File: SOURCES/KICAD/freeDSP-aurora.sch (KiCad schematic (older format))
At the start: 76 parts, among them IC101 IC_ADAU1452, IC102 IC_25AA1024, IC103 IC_TLE2426ID, IC104 IC_ADM811TARTZ, IC105 IC_LM1117MP-5.0, IC106 IC_NCP1117LPST33, IC107 IC_LM1117MP-5.0, Q101 Q_STD2805, X101 MicroMatch14, X102 HDR_02x08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

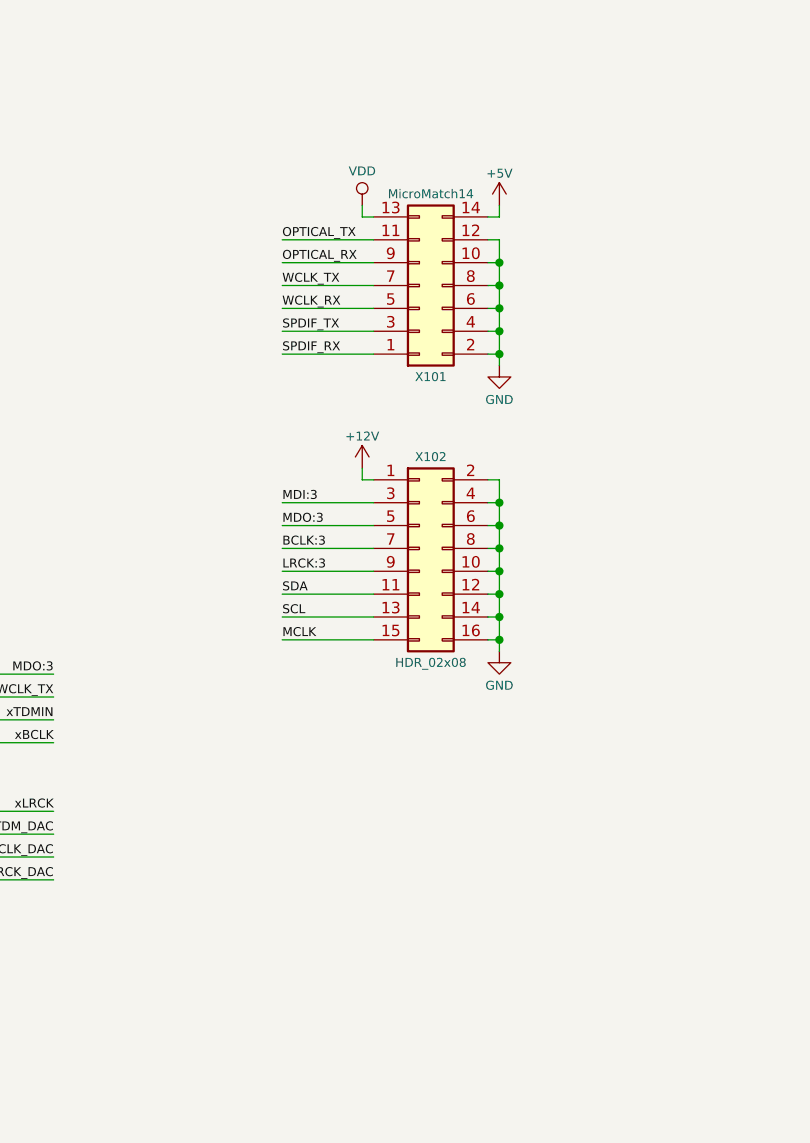
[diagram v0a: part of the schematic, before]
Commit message: Optimized ground plane
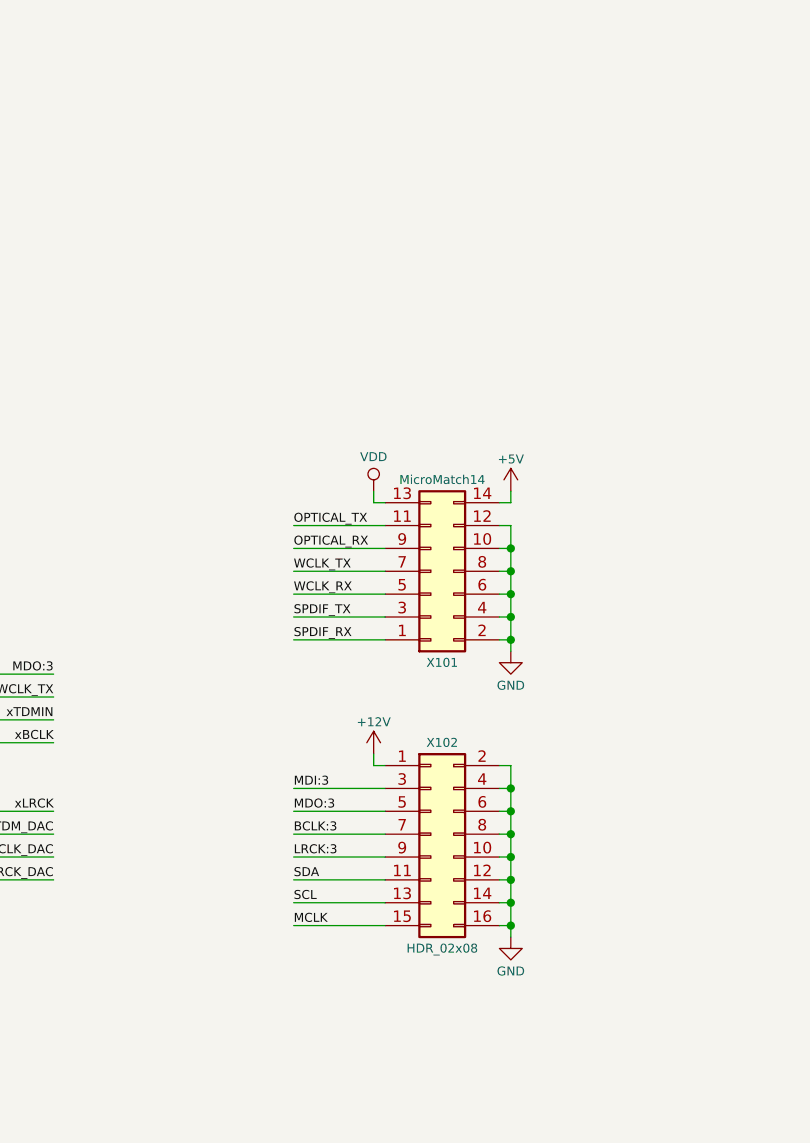
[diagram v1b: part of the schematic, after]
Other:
- moved on the sheet: X101, X102

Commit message: Updated BOM
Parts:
- B101, B102, B103, B104: Manufacturer (none) -> -; pn (none) -> -
- C101: manf_num GRM21BR61E106MA73L -> (none)
- R101, R102, R104, R105: digikey ??? -> TC164J-33CT-ND
- R108: value 100R -> RES_100R_1%_0.125W_Thick_0805; digikey ??? -> 311-100CRCT-ND
- R116: value 560R -> RES_560R_1%_0.125W_Thick_0805; Manufacturer (none) -> Yageo; digikey ??? -> 311-560CRCT-ND; pn (none) -> RC0805FR-07560RL
- X101: digikey ??? -> A110871CT-ND
- X102: digikey ??? -> S2011EC-08-ND
- X103: digikey ??? -> WM1732-ND
- X106: Manufacturer (none) -> Wurth Electronics Inc.; Value1 (none) -> HDR-01x02; Value2 (none) -> -; digikey (none) -> 732-5315-ND; pn (none) -> 61300211121
- Y101: digikey ??? -> SER3690CT-ND
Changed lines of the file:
@@
 F 5 "-" H 0   0   50  0001 C CNN "Value2"
 F 6 "-" H 0   0   50  0001 C CNN "digikey"
+F 7 "-" H 0   0   50  0001 C CNN "Manufacturer"
+F 8 "-" H 0   0   50  0001 C CNN "pn"
 	1    15400 9900
 	1    0    0    -1
@@
 F 5 "-" H 0   0   50  0001 C CNN "Value2"
 F 6 "-" H 0   0   50  0001 C CNN "digikey"
+F 7 "-" H 0   0   50  0001 C CNN "Manufacturer"
+F 8 "-" H 0   0   50  0001 C CNN "pn"
 	1    15550 9900
 	1    0    0    -1
@@
 F 5 "-" H 0   0   50  0001 C CNN "Value2"
 F 6 "-" H 0   0   50  0001 C CNN "digikey"
+F 7 "-" H 0   0   50  0001 C CNN "Manufacturer"
+F 8 "-" H 0   0   50  0001 C CNN "pn"
 	1    15700 9900
 	1    0    0    -1
@@
 F 5 "-" H 0   0   50  0001 C CNN "Value2"
 F 6 "-" H 0   0   50  0001 C CNN "digikey"
+F 7 "-" H 0   0   50  0001 C CNN "Manufacturer"
+F 8 "-" H 0   0   50  0001 C CNN "pn"
 	1    15850 9900
 	1    0    0    -1
@@
 P 7200 6450
 F 0 "R108" V 7200 6450 39  0000 C CNN
-F 1 "100R" V 7275 6450 39  0000 C CNN
+F 1 "RES_100R_1%_0.125W_Thick_0805" V 7275 6450 39  0000 C CNN
 F 2 "rklib:C0805-RES" V 7130 6450 50  0001 C CNN
 F 3 "" H 7200 6450 50  0000 C CNN
 F 4 "100R" H 0   0   50  0001 C CNN "Value1"
 F 5 "1% 0.125W Thick" H 0   0   50  0001 C CNN "Value2"
-F 6 "???" H 0   0   50  0001 C CNN "digikey"
+F 6 "311-100CRCT-ND" H 0   0   50  0001 C CNN "digikey"
 F 7 "Yageo" H 0   0   50  0001 C CNN "Manufacturer"
 F 8 "RC0805FR-07100RL" H 0   0   50  0001 C CNN "pn"
@@
 F 4 "24M576" H 0   0   50  0001 C CNN "Value1"
 F 5 "-" H 0   0   50  0001 C CNN "Value2"
-F 6 "???" H 0   0   50  0001 C CNN "digikey"
+F 6 "SER3690CT-ND" H 0   0   50  0001 C CNN "digikey"
 F 7 "EPSON" H 0   0   50  0001 C CNN "Manufacturer"
 F 8 "FA-238 24.5760MB-K3" H 0   0   50  0001 C CNN "pn"
@@
 F 4 "MicroMatch-14" H 50  1250 50  0001 C CNN "Value1"
 F 5 "-" H 50  1250 50  0001 C CNN "Value2"
-F 6 "???" H 50  1250 50  0001 C CNN "digikey"
+F 6 "A110871CT-ND" H 50  1250 50  0001 C CNN "digikey"
 F 7 "TE Connectivity AMP Connectors" H 50  1250 50  0001 C CNN "Manufacturer"
 F 8 "1-215079-4" H 50  1250 50  0001 C CNN "pn"
@@
 F 4 "HDR_02x08" H 50  1250 50  0001 C CNN "Value1"
 F 5 "-" H 50  1250 50  0001 C CNN "Value2"
-F 6 "???" H 50  1250 50  0001 C CNN "digikey"
+F 6 "S2011EC-08-ND" H 50  1250 50  0001 C CNN "digikey"
 F 7 "Sullins Connector Solutions" H 50  1250 50  0001 C CNN "Manufacturer"
 F 8 "PRPC008DAAN-RC" H 50  1250 50  0001 C CNN "pn"
@@
 F 7 "Murata Electronics North America" H 5650 4800 39  0001 C CNN "Manufacturer"
 F 8 "GRM21BR61E106MA73L" H 5650 4800 39  0001 C CNN "pn"
-F 9 "GRM21BR61E106MA73L" H 5650 4800 50  0001 C CNN "manf_num"
 	1    5650 4800
 	0    1    1    0
@@
 F 4 "33R0" V 7650 3000 39  0000 L CNN "Value1"
 F 5 "5% 62,5mW" H 7400 2700 39  0001 C CNN "Value2"
-F 6 "???" H 7400 2600 39  0001 C CNN "digikey"
+F 6 "TC164J-33CT-ND" H 7400 2600 39  0001 C CNN "digikey"
 F 7 "Yageo" H 0   0   50  0001 C CNN "Manufacturer"
 F 8 "TC164-JR-0733RL" H 0   0   50  0001 C CNN "pn"
@@
 F 4 "33R0" V 8550 3000 39  0000 L CNN "Value1"
 F 5 "5% 62,5mW" H 8300 2700 39  0001 C CNN "Value2"
-F 6 "???" H 8300 2600 39  0001 C CNN "digikey"
+F 6 "TC164J-33CT-ND" H 8300 2600 39  0001 C CNN "digikey"
 F 7 "Yageo" H 0   0   50  0001 C CNN "Manufacturer"
 F 8 "TC164-JR-0733RL" H 0   0   50  0001 C CNN "pn"
@@
 F 4 "33R0" V 9650 4700 39  0000 L CNN "Value1"
 F 5 "5% 62,5mW" H 9400 4400 39  0001 C CNN "Value2"
-F 6 "???" H 9400 4300 39  0001 C CNN "digikey"
+F 6 "TC164J-33CT-ND" H 9400 4300 39  0001 C CNN "digikey"
 F 7 "Yageo" H 0   0   50  0001 C CNN "Manufacturer"
 F 8 "TC164-JR-0733RL" H 0   0   50  0001 C CNN "pn"
@@
 F 4 "33R0" V 9650 5300 39  0000 L CNN "Value1"
 F 5 "5% 62,5mW" H 9400 5000 39  0001 C CNN "Value2"
-F 6 "???" H 9400 4900 39  0001 C CNN "digikey"
+F 6 "TC164J-33CT-ND" H 9400 4900 39  0001 C CNN "digikey"
 F 7 "Yageo" H 0   0   50  0001 C CNN "Manufacturer"
 F 8 "TC164-JR-0733RL" H 0   0   50  0001 C CNN "pn"
@@
 F 4 "PB-01x03" H -3500 1550 50  0001 C CNN "Value1"
 F 5 "-" H -3500 1550 50  0001 C CNN "Value2"
-F 6 "???" H -3500 1550 50  0001 C CNN "digikey"
+F 6 "WM1732-ND" H -3500 1550 50  0001 C CNN "digikey"
 F 7 "Molex, LLC" H -3500 1550 50  0001 C CNN "Manufacturer"
 F 8 "0530470310" H -3500 1550 50  0001 C CNN "pn"
@@
 P 11050 10500
 F 0 "R116" V 11050 10500 39  0000 C CNN
-F 1 "560R" V 11125 10500 39  0000 C CNN
+F 1 "RES_560R_1%_0.125W_Thick_0805" V 11125 10500 39  0000 C CNN
 F 2 "rklib:C0805-RES" V 10980 10500 50  0001 C CNN
 F 3 "" H 11050 10500 50  0000 C CNN
 F 4 "560R" H 3850 4050 50  0001 C CNN "Value1"
 F 5 "1% 0.125W Thick" H 3850 4050 50  0001 C CNN "Value2"
-F 6 "???" H 3850 4050 50  0001 C CNN "digikey"
-F 7 "" H 3850 4050 50  0001 C CNN "Manufacturer"
-F 8 "" H 3850 4050 50  0001 C CNN "pn"
+F 6 "311-560CRCT-ND" H 3850 4050 50  0001 C CNN "digikey"
+F 7 "Yageo" H 0   0   50  0001 C CNN "Manufacturer"
+F 8 "RC0805FR-07560RL" H 0   0   50  0001 C CNN "pn"
 	1    11050 10500
 	1    0    0    -1
@@
 F 2 "rklib:HDR_01x02" H 11250 10700 50  0001 C CNN
 F 3 "~" H 11250 10700 50  0001 C CNN
+F 4 "Wurth Electronics Inc." H 0   0   50  0001 C CNN "Manufacturer"
+F 5 "HDR-01x02" H 0   0   50  0001 C CNN "Value1"
+F 6 "-" H 0   0   50  0001 C CNN "Value2"
+F 7 "732-5315-ND" H 0   0   50  0001 C CNN "digikey"
+F 8 "61300211121" H 0   0   50  0001 C CNN "pn"
 	1    11250 10700
 	1    0    0    -1

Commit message: Bugfix: Made WiFi pins unconnected
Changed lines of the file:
@@
 $EndDescr
 $Sheet
-S 1000 1000 1750 800
+S 1100 900  1750 800
 U 5904EED2
 F0 "AD-Wandler" 39
 F1 "ad.sch" 39
-F2 "MCLK" I L 1000 1100 39
-F3 "BCLK" I L 1000 1200 39
-F4 "LRCK" I L 1000 1300 39
-F5 "TDM" O R 2750 1100 39
-F6 "OVF" O R 2750 1200 39
-F7 "~RST" I L 1000 1400 39
-F8 "VGROUND" I L 1000 1500 39
-F9 "SDA" I L 1000 1600 39
-F10 "SCL" I L 1000 1700 39
+F2 "MCLK" I L 1100 1000 39
+F3 "BCLK" I L 1100 1100 39
+F4 "LRCK" I L 1100 1200 39
+F5 "TDM" O R 2850 1000 39
+F6 "OVF" O R 2850 1100 39
+F7 "~RST" I L 1100 1300 39
+F8 "VGROUND" I L 1100 1400 39
+F9 "SDA" I L 1100 1500 39
+F10 "SCL" I L 1100 1600 39
 $EndSheet
 $Sheet
-S 13800 900  1600 950
+S 13850 900  1750 900
 U 5904EED5
 F0 "DA-Wandler" 39
 F1 "da.sch" 39
-F2 "MCLK" I L 13800 1000 39
-F3 "BCLK" I L 13800 1100 39
-F4 "LRCK" I L 13800 1200 39
-F5 "~RST" I L 13800 1400 39
-F6 "TDM" I L 13800 1300 39
-F7 "VGROUND" I L 13800 1500 39
-F8 "SDA" I L 13800 1600 39
-F9 "SCL" I L 13800 1700 39
+F2 "MCLK" I L 13850 1000 39
+F3 "BCLK" I L 13850 1100 39
+F4 "LRCK" I L 13850 1200 39
+F5 "~RST" I L 13850 1400 39
+F6 "TDM" I L 13850 1300 39
+F7 "VGROUND" I L 13850 1500 39
+F8 "SDA" I L 13850 1600 39
+F9 "SCL" I L 13850 1700 39
 $EndSheet
 $Comp
@@
 Text Label 8200 2550 3    39   ~ 0
 xBCLK
-Text Label 3200 1100 2    39   ~ 0
+Text Label 3300 1000 2    39   ~ 0
 TDM_ADC
-Text Label 600  1300 0    39   ~ 0
+Text Label 700  1200 0    39   ~ 0
 LRCK_ADC
-Text Label 600  1200 0    39   ~ 0
+Text Label 700  1100 0    39   ~ 0
 BCLK_ADC
 Text Label 10000 5500 2    39   ~ 0
@@
 Text Label 10000 4700 2    39   ~ 0
 WCLK_TX
-Text Label 13400 1200 0    39   ~ 0
+Text Label 13450 1200 0    39   ~ 0
 LRCK_DAC
-Text Label 13400 1100 0    39   ~ 0
+Text Label 13450 1100 0    39   ~ 0
 BCLK_DAC
-Text Label 13400 1300 0    39   ~ 0
+Text Label 13450 1300 0    39   ~ 0
 TDM_DAC
 $Comp
@@
 Text Label 12950 9150 2    39   ~ 0
 VGROUND
-Text Label 13400 1500 0    39   ~ 0
+Text Label 13450 1500 0    39   ~ 0
 VGROUND
-Text Label 600  1500 0    39   ~ 0
+Text Label 700  1400 0    39   ~ 0
 VGROUND
-Text Label 600  1400 0    39   ~ 0
+Text Label 700  1300 0    39   ~ 0
 ~RST
-Text Label 13400 1400 0    39   ~ 0
+Text Label 13450 1400 0    39   ~ 0
 ~RST
-Text Label 13400 1000 0    39   ~ 0
+Text Label 13450 1000 0    39   ~ 0
 MCLK
-Text Label 600  1100 0    39   ~ 0
+Text Label 700  1000 0    39   ~ 0
 MCLK
 Text Label 6150 4300 0    39   ~ 0
@@
 	8400 2900 8400 2550
 Wire Wire Line
-	2750 1100 3200 1100
+	2850 1000 3300 1000
 Wire Wire Line
-	1000 1300 600  1300
+	1100 1200 700  1200
 Wire Wire Line
-	1000 1200 600  1200
+	1100 1100 700  1100
 Wire Wire Line
 	8950 5300 9200 5300
@@
 	8950 5000 9150 5000
 Wire Wire Line
-	13800 1200 13400 1200
+	13850 1200 13450 1200
 Wire Wire Line
-	13800 1100 13400 1100
+	13850 1100 13450 1100
 Wire Wire Line
-	13800 1300 13400 1300
+	13850 1300 13450 1300
 Wire Wire Line
 	8950 5400 9200 5400
@@
 	11600 9200 11600 9250
 Wire Wire Line
-	13800 1500 13400 1500
+	13850 1500 13450 1500
 Wire Wire Line
-	1000 1500 600  1500
+	1100 1400 700  1400
 Wire Wire Line
-	1000 1400 600  1400
+	1100 1300 700  1300
 Wire Wire Line
-	13800 1400 13400 1400
+	13850 1400 13450 1400
 Wire Wire Line
-	13800 1000 13400 1000
+	13850 1000 13450 1000
 Wire Wire Line
-	1000 1100 600  1100
+	1100 1000 700  1000
 Wire Wire Line
 	6550 4300 6150 4300
@@
 	4800 5550 5050 5550
 $Sheet
-S 1200 2850 2250 1750
+S 1100 1950 1750 1100
 U 5B770691
 F0 "XMOS" 39
 F1 "xmos.sch" 39
-F2 "XTDMOUT4" O R 3450 3350 39
-F3 "XTDMOUT3" O R 3450 3250 39
-F4 "XTDMOUT2" O R 3450 3150 39
-F5 "XTDMOUT1" O R 3450 3050 39
-F6 "XTDMIN4" I L 1200 3350 39
-F7 "XTDMIN3" I L 1200 3250 39
-F8 "XTDMIN2" I L 1200 3150 39
-F9 "XTDMIN1" I L 1200 3050 39
-F10 "XBCLK" B L 1200 3450 39
-F11 "XLRCK" B L 1200 3550 39
-F12 "SCL" O R 3450 3450 39
-F13 "SDA" O R 3450 3550 39
-F14 "~RST" I L 1200 3850 39
-F15 "OPTICAL_TX" O R 3450 3650 39
-F16 "OPTICAL_RX" I L 1200 3650 39
-F17 "MCLK" I L 1200 2950 39
-F18 "WCLKIN" I L 1200 3750 39
+F2 "XTDMOUT4" O R 2850 2450 39
+F3 "XTDMOUT3" O R 2850 2350 39
+F4 "XTDMOUT2" O R 2850 2250 39
+F5 "XTDMOUT1" O R 2850 2150 39
+F6 "XTDMIN4" I L 1100 2450 39
+F7 "XTDMIN3" I L 1100 2350 39
+F8 "XTDMIN2" I L 1100 2250 39
+F9 "XTDMIN1" I L 1100 2150 39
+F10 "XBCLK" B L 1100 2550 39
+F11 "XLRCK" B L 1100 2650 39
+F12 "SCL" O R 2850 2550 39
+F13 "SDA" O R 2850 2650 39
+F14 "~RST" I L 1100 2950 39
+F15 "OPTICAL_TX" O R 2850 2750 39
+F16 "OPTICAL_RX" I L 1100 2750 39
+F17 "MCLK" I L 1100 2050 39
+F18 "WCLKIN" I L 1100 2850 39
 $EndSheet
-$Sheet
-S 1300 5300 2350 1450
-U 5B77113C
-F0 "ESP32" 39
-F1 "esp.sch" 39
-F2 "MOSI" O R 3650 5400 39
-F3 "MISO" I R 3650 5500 39
-F4 "SCK" O R 3650 5600 39
-F5 "CS" O R 3650 5700 39
-F6 "BCLK" O R 3650 5800 39
-F7 "LRCK" O R 3650 5900 39
-F8 "SDATA" O R 3650 6000 39
-F9 "~MRST" O R 3650 6500 39
-F10 "SCL1" O R 3650 6100 39
-F11 "SDA1" B R 3650 6200 39
-F12 "SCL2" O R 3650 6300 39
-F13 "SDA2" B R 3650 6400 39
-$EndSheet
-Text Label 800  2950 0    39   ~ 0
+Text Label 700  2050 0    39   ~ 0
 MCLK
 Wire Wire Line
-	1200 2950 800  2950
-Text Label 800  3050 0    39   ~ 0
+	1100 2050 700  2050
+Text Label 700  2150 0    39   ~ 0
 xTDMIN
 Wire Wire Line
-	1200 3050 800  3050
-Text Label 3850 3050 2    39   ~ 0
+	1100 2150 700  2150
+Text Label 3250 2150 2    39   ~ 0
 xTDMOUT
 Wire Wire Line
-	3450 3050 3850 3050
-Text Label 800  3550 0    39   ~ 0
+	2850 2150 3250 2150
+Text Label 700  2650 0    39   ~ 0
 xLRCK
-Text Label 800  3450 0    39   ~ 0
+Text Label 700  2550 0    39   ~ 0
 xBCLK
 Wire Wire Line
-	1200 3550 800  3550
+	1100 2650 700  2650
 Wire Wire Line
-	1200 3450 800  3450
-Text Label 800  3850 0    39   ~ 0
+	1100 2550 700  2550
+Text Label 700  2950 0    39   ~ 0
 ~RST
 Wire Wire Line
-	1200 3850 800  3850
-Text Label 800  3750 0    39   ~ 0
+	1100 2950 700  2950
+Text Label 700  2850 0    39   ~ 0
 WCLK_RX
 Wire Wire Line
-	1200 3750 800  3750
-Text Label 800  3650 0    39   ~ 0
+	1100 2850 700  2850
+Text Label 700  2750 0    39   ~ 0
 OPTICAL_RX
 Wire Wire Line
-	1200 3650 800  3650
+	1100 2750 700  2750
 Text Label 11050 4350 0    39   ~ 0
 SPDIF_TX
@@
 Wire Wire Line
 	11450 4350 11050 4350
-Text Label 3850 3650 2    39   ~ 0
+Text Label 3250 2750 2    39   ~ 0
 OPTICAL_TX
 Wire Wire Line
-	3450 3650 3850 3650
-Text Label 3850 3550 2    39   ~ 0
+	2850 2750 3250 2750
+Text Label 3250 2650 2    39   ~ 0
 xSDA
 Wire Wire Line
-	3450 3550 3850 3550
-Text Label 3850 3450 2    39   ~ 0
+	2850 2650 3250 2650
+Text Label 3250 2550 2    39   ~ 0
 xSCL
 Wire Wire Line
-	3450 3450 3850 3450
+	2850 2550 3250 2550
 $Comp
 L freeDSP-aurora-rescue:Conn_02x07_Odd_Even X101
@@
 	11950 5000 12000 5000
 Connection ~ 12000 5100
-Text Label 4050 6200 2    39   ~ 0
+Text Label 3250 3800 2    39   ~ 0
 SDA
 Wire Wire Line
-	3650 6200 4050 6200
-Text Label 4050 6100 2    39   ~ 0
+	2850 3800 3250 3800
+Text Label 3250 3700 2    39   ~ 0
 SCL
 Wire Wire Line
-	3650 6100 4050 6100
-Text Label 4050 6500 2    39   ~ 0
+	2850 3700 3250 3700
+Text Label 3250 4100 2    39   ~ 0
 ~USBRST
 Wire Wire Line
-	3650 6500 4050 6500
-Text Label 4050 6000 2    39   ~ 0
+	2850 4100 3250 4100
+Text Label 3250 3600 2    39   ~ 0
 MDI:2
 Wire Wire Line
-	3650 6000 4050 6000
-Text Label 4050 5900 2    39   ~ 0
+	2850 3600 3250 3600
+Text Label 3250 3500 2    39   ~ 0
 LRCK:2
 Wire Wire Line
-	3650 5900 4050 5900
-Text Label 4050 5800 2    39   ~ 0
+	2850 3500 3250 3500
+Text Label 3250 3400 2    39   ~ 0
 BCLK:2
 Wire Wire Line
-	3650 5800 4050 5800
+	2850 3400 3250 3400
 Wire Wire Line
 	600  10300 650  10300
@@
 	1    0    0    -1
 $EndComp
-Text Label 4050 6400 2    39   ~ 0
+Text Label 3250 4000 2    39   ~ 0
 xSDA
 Wire Wire Line
-	3650 6400 4050 6400
-Text Label 4050 6300 2    39   ~ 0
+	2850 4000 3250 4000
+Text Label 3250 3900 2    39   ~ 0
 xSCL
 Wire Wire Line
-	3650 6300 4050 6300
+	2850 3900 3250 3900
 $Comp
 L freeDSP-aurora-rescue:CAP_330u_20%_35V_ALUM_RADIAL C126
@@
 	-1   0    0    -1
 $EndComp
-Text Label 600  1600 0    39   ~ 0
+Text Label 700  1500 0    39   ~ 0
 SDA
 Wire Wire Line
-	1000 1600 600  1600
-Text Label 600  1700 0    39   ~ 0
+	1100 1500 700  1500
+Text Label 700  1600 0    39   ~ 0
 SCL
 Wire Wire Line
-	1000 1700 600  1700
-Text Label 13400 1600 0    39   ~ 0
+	1100 1600 700  1600
+Text Label 13450 1600 0    39   ~ 0
 SDA
 Wire Wire Line
-	13800 1600 13400 1600
-Text Label 13400 1700 0    39   ~ 0
+	13850 1600 13450 1600
+Text Label 13450 1700 0    39   ~ 0
 SCL
 Wire Wire Line
-	13800 1700 13400 1700
+	13850 1700 13450 1700
 $Comp
 L freeDSP-aurora-rescue:R R116
@@
 	5850 10400 5850 10450
 Connection ~ 5600 10400
+$Sheet
+S 1100 3300 1750 900
+U 5B77113C
+F0 "ESP32" 39
+F1 "esp.sch" 39
+F6 "BCLK" O R 2850 3400 39
+F7 "LRCK" O R 2850 3500 39
+F8 "SDATA" O R 2850 3600 39
+F9 "~MRST" O R 2850 4100 39
+F10 "SCL1" O R 2850 3700 39
+F11 "SDA1" B R 2850 3800 39
+F12 "SCL2" O R 2850 3900 39
+F13 "SDA2" B R 2850 4000 39
+$EndSheet
 $EndSCHEMATC
